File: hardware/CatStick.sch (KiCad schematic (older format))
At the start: 70 parts, among them J2 U.FL, J3 USB_B_Micro, J4 Conn_02x05_Odd_Even, J5 Conn_01x04, Q1 DMN6140L, SW1 SW_Push, SW2 RST, U1 CC1352R1F3RGZR, U2 AP2112K-3.3, U3 RFSW8006QTR7, U4 0900FM15D0039, U5 0900PC15A0036, U6 PE4259 RF Switch, U7 ATSAMD21E18A-A, U8 SX1262IMLTRT, Y1 32.768kHz, Y2 48MHz, Y3 32Mhz_10pF_10ppm

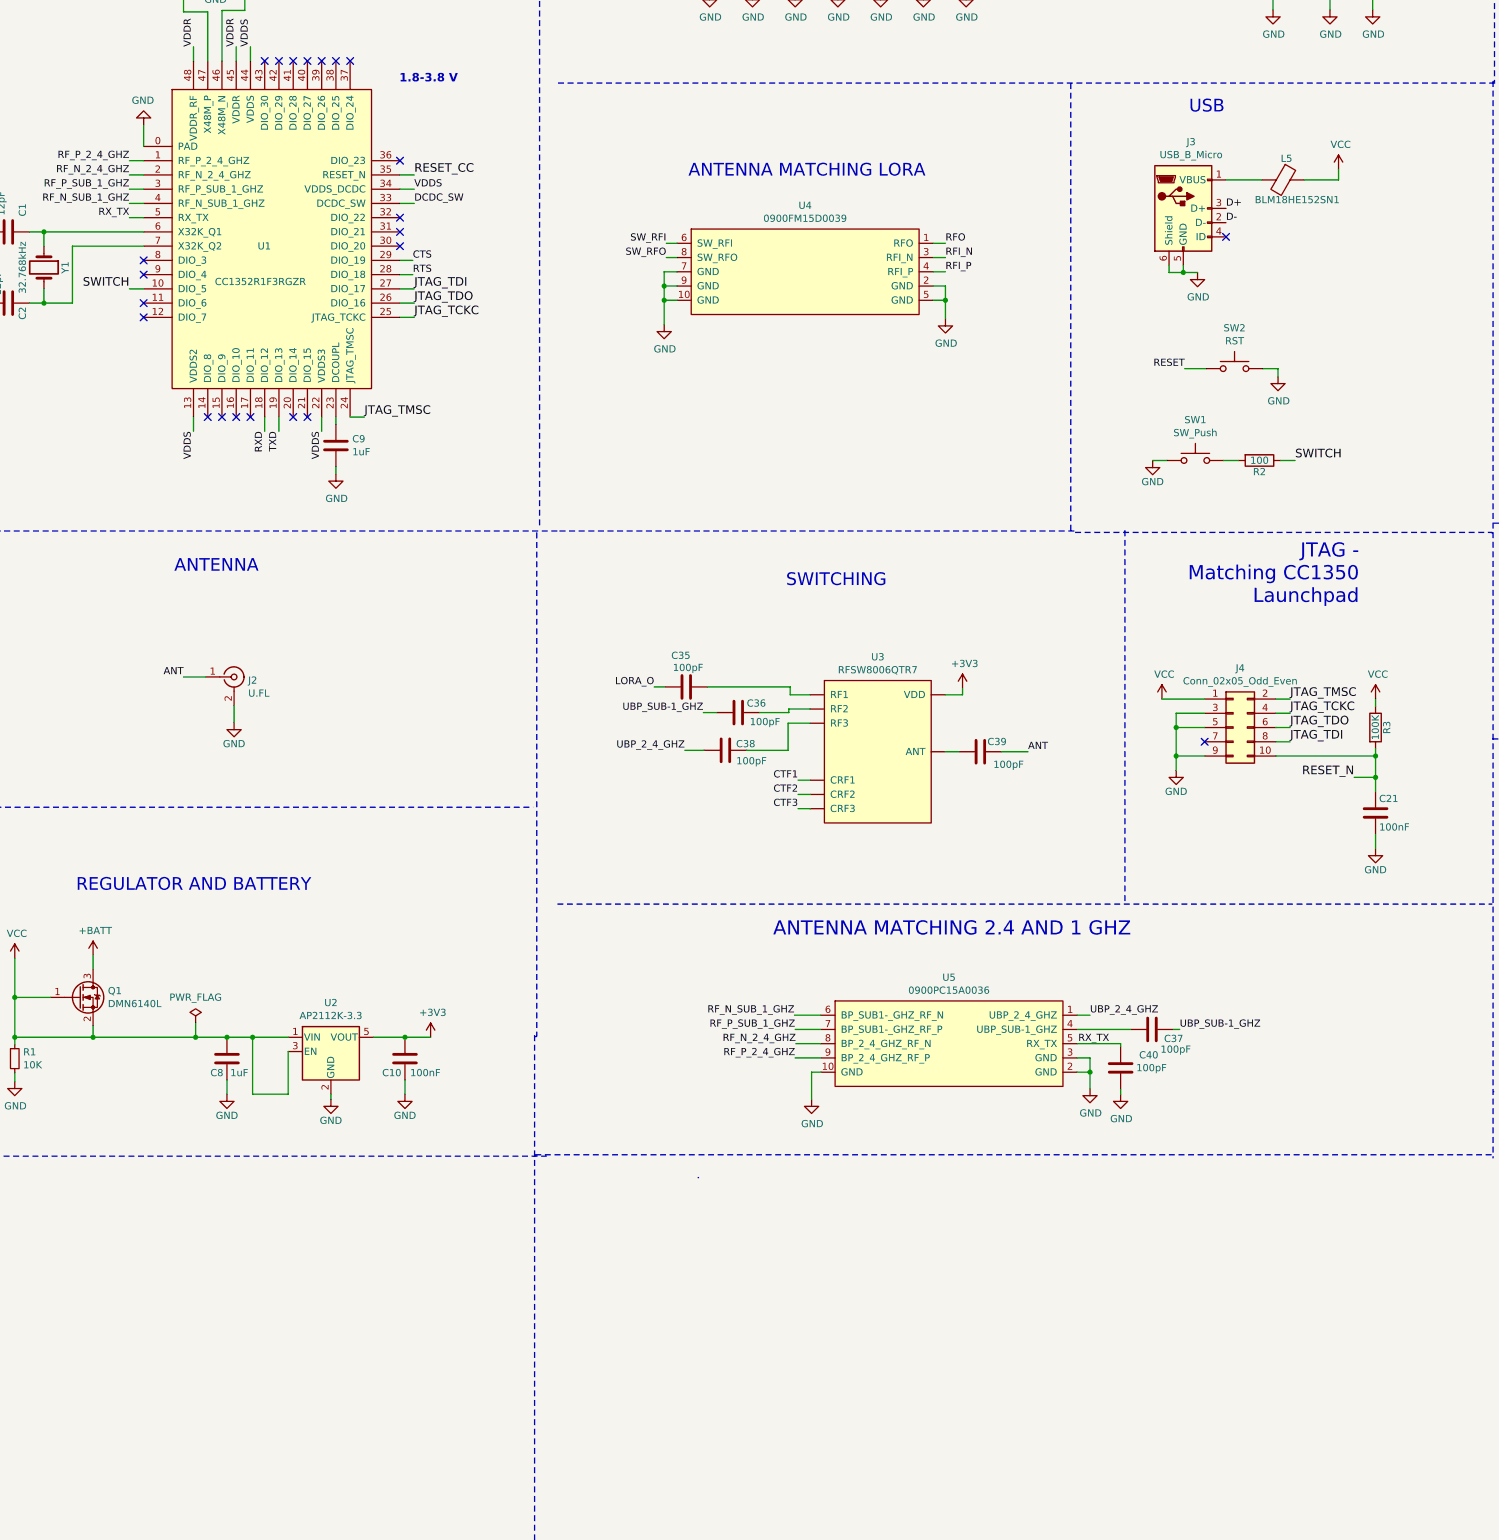
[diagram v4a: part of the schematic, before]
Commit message: addUSBC
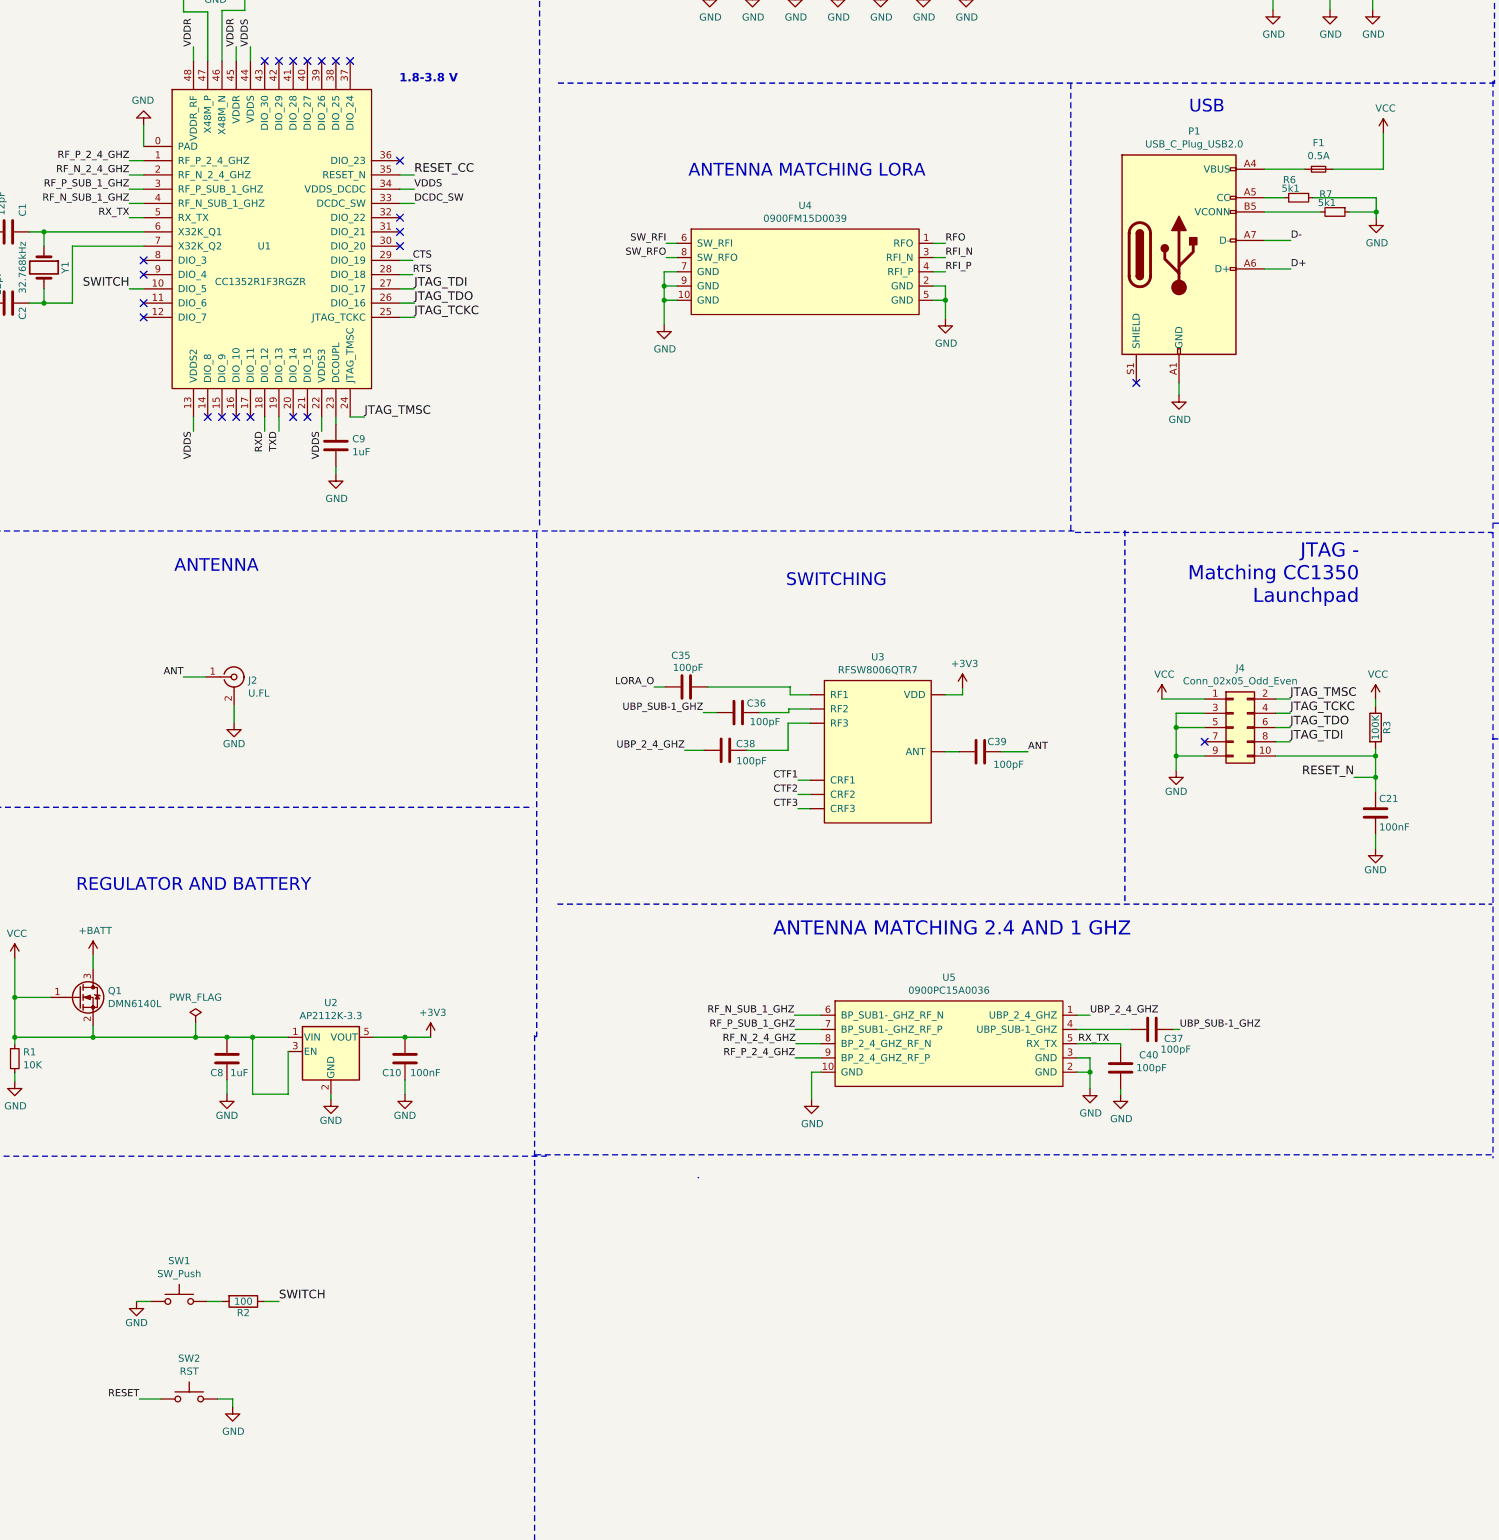
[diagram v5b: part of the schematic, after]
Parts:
- removed J3: USB_B_Micro, Connector_USB:USB_Mini-B_Lumberg_2486_01_Horizontal, symbol CatStick-rescue:USB_B_Micro-Connector-CatStick-rescue
- removed L5: BLM18HE152SN1, Inductor_SMD:L_0603_1608Metric, symbol Device:Ferrite_Bead
- added F1: 0.5A, symbol Device:Fuse_Small
- added P1: USB_C_Plug_USB2.0, symbol Connector:USB_C_Plug_USB2.0
- added R6, R7: 5k1, symbol Device:R_Small
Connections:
- net D+: now also P1.A6 (D+)
- net D-: now also P1.A7 (D-)
- net GND: now also P1.A1 (GND), P1.A12 (GND), P1.B1 (GND), P1.B12 (GND), R6.1, R7.1
- net VCC: now also F1.2
- new net: F1.1, P1.A4 (VBUS), P1.A9 (VBUS), P1.B4 (VBUS), P1.B9 (VBUS)
- new net: P1.A5 (CC), R6.2
- new net: P1.B5 (VCONN), R7.2
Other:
- moved on the sheet: R2, SW1, SW2
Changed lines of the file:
@@
-$EndComp
-$Comp
-L Device:Ferrite_Bead L5
-U 1 1 58C79DB4
-P 10290 3130
-F 0 "L5" V 10140 3155 50  0000 C CNN
-F 1 "BLM18HE152SN1" V 10430 3230 50  0000 C CNN
-F 2 "Inductor_SMD:L_0603_1608Metric" V 10220 3130 50  0001 C CNN
-F 3 "" H 10290 3130 50  0000 C CNN
-	1    10290 3130
-	0    1    1    0
 $EndComp
 $Comp
@@
 L power:GND #PWR035
 U 1 1 58CC4391
-P 9375 5100
-F 0 "#PWR035" H 9375 4850 50  0001 C CNN
-F 1 "GND" H 9375 4950 50  0000 C CNN
-F 2 "" H 9375 5100 50  0000 C CNN
-F 3 "" H 9375 5100 50  0000 C CNN
-	1    9375 5100
+P 2240 11005
+F 0 "#PWR035" H 2240 10755 50  0001 C CNN
+F 1 "GND" H 2240 10855 50  0000 C CNN
+F 2 "" H 2240 11005 50  0000 C CNN
+F 3 "" H 2240 11005 50  0000 C CNN
+	1    2240 11005
 	1    0    0    -1
 $EndComp
@@
 L Device:R R2
 U 1 1 58CC4456
-P 10125 5100
-F 0 "R2" V 10205 5100 50  0000 C CNN
-F 1 "100" V 10125 5100 50  0000 C CNN
-F 2 "Resistor_SMD:R_0603_1608Metric" V 10055 5100 50  0001 C CNN
-F 3 "" H 10125 5100 50  0000 C CNN
-	1    10125 5100
+P 2990 11005
+F 0 "R2" V 3070 11005 50  0000 C CNN
+F 1 "100" V 2990 11005 50  0000 C CNN
+F 2 "Resistor_SMD:R_0603_1608Metric" V 2920 11005 50  0001 C CNN
+F 3 "" H 2990 11005 50  0000 C CNN
+	1    2990 11005
 	0    1    1    0
 $EndComp
-Text Label 10375 5100 0    60   ~ 0
+Text Label 3240 11005 0    60   ~ 0
 SWITCH
 Text Label 2190 3895 2    60   ~ 0
@@
 	5515 1365 5415 1365
 Wire Wire Line
-	9890 3130 10140 3130
-Wire Wire Line
 	2875 9550 2875 9450
 Wire Wire Line
@@
 	745  8695 745  8795
 Wire Wire Line
-	9375 5100 9475 5100
-Wire Wire Line
-	9875 5100 9975 5100
-Wire Wire Line
-	10375 5100 10275 5100
+	2240 11005 2340 11005
+Wire Wire Line
+	2740 11005 2840 11005
+Wire Wire Line
+	3240 11005 3140 11005
 Wire Wire Line
 	2655 9050 2655 9150
@@
 L Switch:SW_Push SW1
 U 1 1 5BAA6E6C
-P 9675 5100
-F 0 "SW1" H 9675 5385 50  0000 C CNN
-F 1 "SW_Push" H 9675 5294 50  0000 C CNN
-F 2 "cc1350:SKSLLAE010" H 9675 5300 50  0001 C CNN
-F 3 "" H 9675 5300 50  0001 C CNN
-	1    9675 5100
-	1    0    0    -1
-$EndComp
-$Comp
-L CatStick-rescue:USB_B_Micro-Connector-CatStick-rescue J3
-U 1 1 5BABCCC6
-P 9590 3330
-F 0 "J3" H 9645 3797 50  0000 C CNN
-F 1 "USB_B_Micro" H 9645 3706 50  0000 C CNN
-F 2 "Connector_USB:USB_Mini-B_Lumberg_2486_01_Horizontal" H 9740 3280 50  0001 C CNN
-F 3 "~" H 9740 3280 50  0001 C CNN
-	1    9590 3330
-	1    0    0    -1
-$EndComp
-$Comp
-L power:GND #PWR038
-U 1 1 5BAE7F9A
-P 9690 3780
-F 0 "#PWR038" H 9690 3530 50  0001 C CNN
-F 1 "GND" H 9695 3607 50  0000 C CNN
-F 2 "" H 9690 3780 50  0001 C CNN
-F 3 "" H 9690 3780 50  0001 C CNN
-	1    9690 3780
-	1    0    0    -1
-$EndComp
-NoConn ~ 9890 3530
-Wire Wire Line
-	9690 3780 9590 3780
-Wire Wire Line
-	9490 3780 9490 3730
-Wire Wire Line
-	9590 3730 9590 3780
-Connection ~ 9590 3780
-Wire Wire Line
-	9590 3780 9490 3780
+P 2540 11005
+F 0 "SW1" H 2540 11290 50  0000 C CNN
+F 1 "SW_Push" H 2540 11199 50  0000 C CNN
+F 2 "cc1350:SKSLLAE010" H 2540 11205 50  0001 C CNN
+F 3 "" H 2540 11205 50  0001 C CNN
+	1    2540 11005
+	1    0    0    -1
+$EndComp
 Text Notes 6710 8450 0    99   ~ 0
 ANTENNA MATCHING 2.4 AND 1 GHZ
@@
 	1    0    0    -1
 $EndComp
-Text Label 9890 3330 0    50   ~ 0
-D+
-Text Label 9890 3430 0    50   ~ 0
-D-
 Wire Notes Line
 	5195 5595 645  5595
@@
 Wire Notes Line
 	11765 2435 11765 10000
-Wire Wire Line
-	10440 3130 10680 3130
-Wire Wire Line
-	10680 3130 10680 3055
 $Comp
 L power:VCC #PWR044
 U 1 1 5FA2D547
-P 10680 3055
-F 0 "#PWR044" H 10680 2905 50  0001 C CNN
-F 1 "VCC" H 10695 3228 50  0000 C CNN
-F 2 "" H 10680 3055 50  0001 C CNN
-F 3 "" H 10680 3055 50  0001 C CNN
-	1    10680 3055
+P 10995 2800
+F 0 "#PWR044" H 10995 2650 50  0001 C CNN
+F 1 "VCC" H 11010 2973 50  0000 C CNN
+F 2 "" H 10995 2800 50  0001 C CNN
+F 3 "" H 10995 2800 50  0001 C CNN
+	1    10995 2800
 	1    0    0    -1
 $EndComp
@@
 L Switch:SW_Push SW2
 U 1 1 5FD003C3
-P 9950 4455
-F 0 "SW2" H 9950 4740 50  0000 C CNN
-F 1 "RST" H 9950 4649 50  0000 C CNN
-F 2 "" H 9950 4655 50  0001 C CNN
-F 3 "~" H 9950 4655 50  0001 C CNN
-	1    9950 4455
-	1    0    0    -1
-$EndComp
-Text Label 9600 4455 2    50   ~ 0
+P 2610 11690
+F 0 "SW2" H 2610 11975 50  0000 C CNN
+F 1 "RST" H 2610 11884 50  0000 C CNN
+F 2 "" H 2610 11890 50  0001 C CNN
+F 3 "~" H 2610 11890 50  0001 C CNN
+	1    2610 11690
+	1    0    0    -1
+$EndComp
+Text Label 2260 11690 2    50   ~ 0
 RESET
 Wire Wire Line
-	9600 4455 9750 4455
+	2260 11690 2410 11690
 $Comp
 L power:GND #PWR042
 U 1 1 5FD0172F
-P 10255 4510
-F 0 "#PWR042" H 10255 4260 50  0001 C CNN
-F 1 "GND" H 10260 4337 50  0000 C CNN
-F 2 "" H 10255 4510 50  0001 C CNN
-F 3 "" H 10255 4510 50  0001 C CNN
-	1    10255 4510
-	1    0    0    -1
-$EndComp
-Wire Wire Line
-	10255 4455 10255 4510
-Wire Wire Line
-	10150 4455 10255 4455
+P 2915 11745
+F 0 "#PWR042" H 2915 11495 50  0001 C CNN
+F 1 "GND" H 2920 11572 50  0000 C CNN
+F 2 "" H 2915 11745 50  0001 C CNN
+F 3 "" H 2915 11745 50  0001 C CNN
+	1    2915 11745
+	1    0    0    -1
+$EndComp
+Wire Wire Line
+	2915 11690 2915 11745
+Wire Wire Line
+	2810 11690 2915 11690
 $Comp
 L SX1262IMLTRT:SX1262IMLTRT U8
@@
 NoConn ~ 16495 3325
 NoConn ~ 16645 5125
+$Comp
+L power:GND #PWR067
+U 1 1 6083ACE2
+P 9560 4640
+F 0 "#PWR067" H 9560 4390 50  0001 C CNN
+F 1 "GND" H 9565 4467 50  0000 C CNN
+F 2 "" H 9560 4640 50  0001 C CNN
+F 3 "" H 9560 4640 50  0001 C CNN
+	1    9560 4640
+	1    0    0    -1
+$EndComp
+Wire Wire Line
+	9560 4640 9560 4555
+Text Label 10345 3755 0    50   ~ 0
+D+
+Text Label 10345 3555 0    50   ~ 0
+D-
+$Comp
+L Connector:USB_C_Plug_USB2.0 P1
+U 1 1 609EE31D
+P 9560 3655
+F 0 "P1" H 9667 4522 50  0000 C CNN
+F 1 "USB_C_Plug_USB2.0" H 9667 4431 50  0000 C CNN
+F 2 "" H 9710 3655 50  0001 C CNN
+F 3 "https://www.usb.org/sites/default/files/documents/usb_type-c.zip" H 9710 3655 50  0001 C CNN
+	1    9560 3655
+	1    0    0    -1
+$EndComp
+Wire Wire Line
+	10345 3755 10160 3755
+Wire Wire Line
+	10345 3555 10160 3555
+Wire Wire Line
+	10995 3055 10995 2800
+$Comp
+L Device:R_Small R6
+U 1 1 60AD7135
+P 10400 3255
+F 0 "R6" V 10275 3145 50  0000 L CNN
+F 1 "5k1" V 10335 3135 50  0000 L CNN
+F 2 "" H 10400 3255 50  0001 C CNN
+F 3 "~" H 10400 3255 50  0001 C CNN
+	1    10400 3255
+	0    1    1    0
+$EndComp
+$Comp
+L Device:R_Small R7
+U 1 1 60AD852A
+P 10655 3355
+F 0 "R7" V 10530 3245 50  0000 L CNN
+F 1 "5k1" V 10590 3235 50  0000 L CNN
+F 2 "" H 10655 3355 50  0001 C CNN
+F 3 "~" H 10655 3355 50  0001 C CNN
+	1    10655 3355
+	0    1    1    0
+$EndComp
+$Comp
+L power:GND #PWR038
+U 1 1 60AD8CC8
+P 10945 3400
+F 0 "#PWR038" H 10945 3150 50  0001 C CNN
+F 1 "GND" H 10950 3227 50  0000 C CNN
+F 2 "" H 10945 3400 50  0001 C CNN
+F 3 "" H 10945 3400 50  0001 C CNN
+	1    10945 3400
+	1    0    0    -1
+$EndComp
+Wire Wire Line
+	10160 3255 10300 3255
+Wire Wire Line
+	10160 3355 10555 3355
+Wire Wire Line
+	10500 3255 10945 3255
+Wire Wire Line
+	10945 3255 10945 3355
+Wire Wire Line
+	10755 3355 10945 3355
+Connection ~ 10945 3355
+Wire Wire Line
+	10945 3355 10945 3400
+NoConn ~ 9260 4555
+$Comp
+L Device:Fuse_Small F1
+U 1 1 60BA6CB5
+P 10540 3055
+F 0 "F1" H 10540 3240 50  0000 C CNN
+F 1 "0.5A" H 10540 3149 50  0000 C CNN
+F 2 "" H 10540 3055 50  0001 C CNN
+F 3 "~" H 10540 3055 50  0001 C CNN
+	1    10540 3055
+	1    0    0    -1
+$EndComp
+Wire Wire Line
+	10640 3055 10995 3055
+Wire Wire Line
+	10160 3055 10440 3055
 $EndSCHEMATC

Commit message: addComponents&footprints
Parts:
- F1: footprint (none) -> Fuse:Fuse_0603_1608Metric_Pad1.05x0.95mm_HandSolder; Mouser# (none) -> 594-MFU0805FF00500P1; manf# (none) -> MFU0805FF00500P100; provedor (none) -> Mouser
- J2: value U.FL -> Antenna; footprint cc1350:U.FL_Hirose_U.FL-R-SMT-1_Vertical -> bast-wan:SMA_EDGE
- J4: footprint cc1350:Pin_Header_Straight_SMT_02x05_1_27mm -> Connector_PinHeader_1.00mm:PinHeader_2x05_P1.00mm_Vertical
- J5: footprint (none) -> Connector_PinHeader_1.00mm:PinHeader_1x04_P1.00mm_Vertical
- L1: footprint Inductor_SMD:L_0402_1005Metric -> Inductor_SMD:L_0603_1608Metric_Pad1.05x0.95mm_HandSolder; LCSC# (none) -> C395094; Mouser# (none) -> (none); manf# (none) -> VHF160808H9N1JT; provedor (none) -> LCSC
- L3: value BLM18HE152SN1 -> BLM18HE152SN1D; footprint Inductor_SMD:L_0603_1608Metric -> Inductor_SMD:L_0603_1608Metric_Pad1.05x0.95mm_HandSolder; Mouser# (none) -> 81-BLM18HE152SN1D; manf# (none) -> BLM18HE152SN1D; provedor (none) -> Mouser
- L4: footprint Inductor_SMD:L_0805_2012Metric -> Inductor_SMD:L_0603_1608Metric_Pad1.05x0.95mm_HandSolder; LCSC# (none) -> C75929; manf# (none) -> SDFL1608S6R8KTF; provedor (none) -> LCSC
- L6: footprint (none) -> Inductor_SMD:L_0603_1608Metric_Pad1.05x0.95mm_HandSolder; LCSC# (none) -> C57838; manf# (none) -> SDFL1608T150KTF; provedor (none) -> LCSC
- L7: footprint (none) -> Inductor_SMD:L_0603_1608Metric_Pad1.05x0.95mm_HandSolder; LCSC# (none) -> C433019; manf# (none) -> MLG0603P47NHT000; provedor (none) -> LCSC
- P1: footprint (none) -> Connectors:C393939; LCSC# (none) -> C393939; manf# (none) -> TYPE-C16PIN; provedor (none) -> LCSC
- Q1: Mouser# (none) -> 621-DMN6140L-13; manf# (none) -> DMN6140L-13; provedor (none) -> Mouser
- R1: footprint (none) -> Resistor_SMD:R_0603_1608Metric_Pad0.98x0.95mm_HandSolder; LCSC# (none) -> C304079; manf# (none) -> AR03FTD1002; provedor (none) -> LCSC
- R2: value 100 -> 100K; footprint Resistor_SMD:R_0603_1608Metric -> Resistor_SMD:R_0603_1608Metric_Pad0.98x0.95mm_HandSolder; LCSC# (none) -> C179820; manf# (none) -> RT0603FRD07100KL; provedor (none) -> LCSC
- R3: footprint Resistor_SMD:R_0603_1608Metric -> Resistor_SMD:R_0603_1608Metric_Pad0.98x0.95mm_HandSolder; LCSC# (none) -> C179820; manf# (none) -> RT0603FRD07100KL; provedor (none) -> LCSC
- R4, R5: footprint (none) -> Resistor_SMD:R_0603_1608Metric_Pad0.98x0.95mm_HandSolder; LCSC# (none) -> C700506; manf# (none) -> RT0603DRD07100RL; provedor (none) -> LCSC
- R6, R7: footprint (none) -> Resistor_SMD:R_0603_1608Metric_Pad0.98x0.95mm_HandSolder; LCSC# (none) -> C319561; manf# (none) -> AR03DTCX5101; provedor (none) -> LCSC
- SW1: footprint cc1350:SKSLLAE010 -> Button_Switch_SMD:SW_SPST_TL3342; LCSC# (none) -> C318889; manf# (none) -> TS-1187A-C-C-B; provedor (none) -> LCSC
- SW2: LCSC# (none) -> C318889; manf# (none) -> TS-1187A-C-C-B; provedor (none) -> LCSC
- U1: footprint cc1352:CC1352R1F3RGZR -> Package_DFN_QFN:VQFN-48-1EP_7x7mm_P0.5mm_EP5.15x5.15mm; LCSC# (none) -> 595-CC1352P1F3RGZR; Mouser# (none) -> 595-CC1352R1F3RGZR; manf# (none) -> CC1352R1F3RGZR; provedor (none) -> Mouser
- U2: LCSC# (none) -> C51118; manf# (none) -> AP2112K-3.3TRG1; provedor (none) -> LCSC
- U3: Mouser# (none) -> 772-RFSW8006QTR7; manf# 772-RFSW8006QTR7 -> RFSW8006QTR7; provedor (none) -> Mouser
- U4: Mouser# (none) -> 609-0900FM15D0039E; manf# (none) -> 0900FM15D0039E; provedor (none) -> Mouser
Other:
- note added: "BUTTONS\n"
- moved on the sheet: R2, SW1, SW2
